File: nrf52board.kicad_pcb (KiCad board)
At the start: 2 copper layers, 10 parts, among them J1 Conn_01x04, U1 nrf52board, U2 E73-2G4M04S

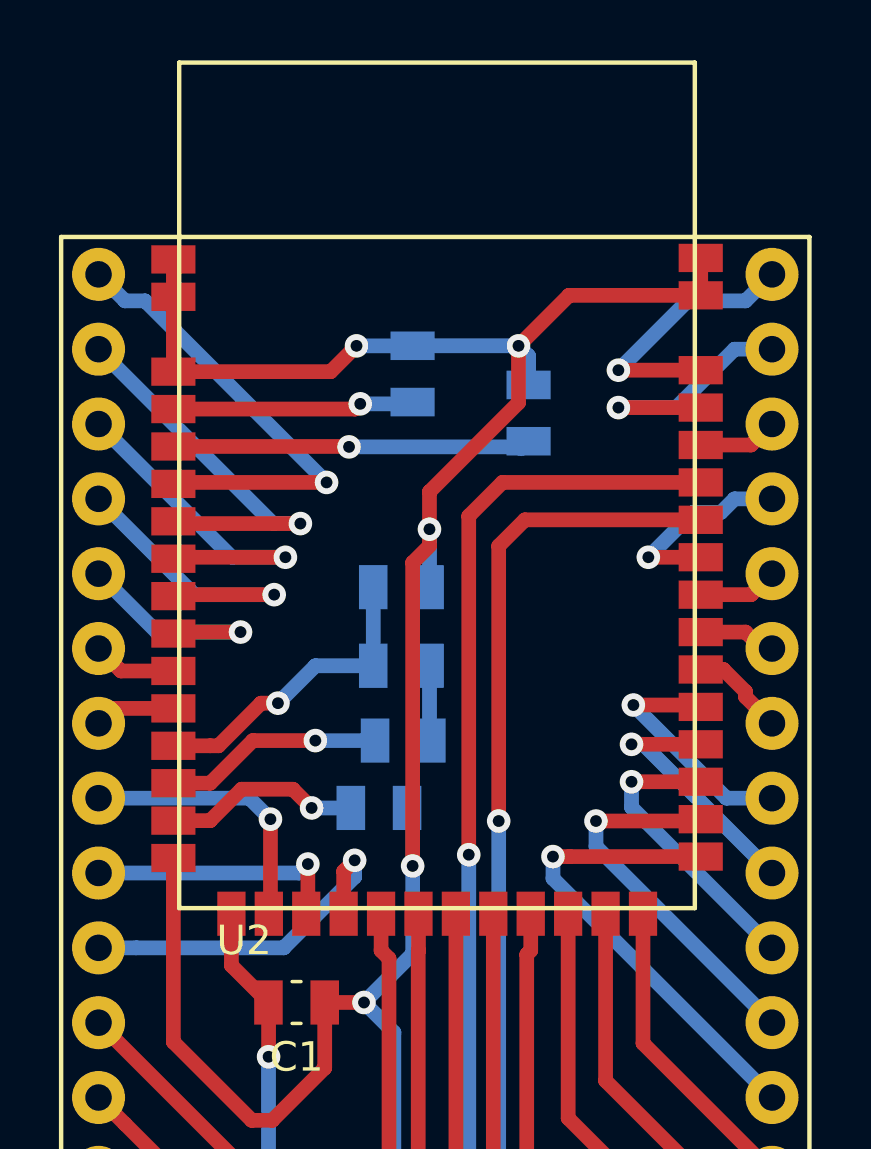
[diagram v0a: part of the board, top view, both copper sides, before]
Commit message: updated module foorptint
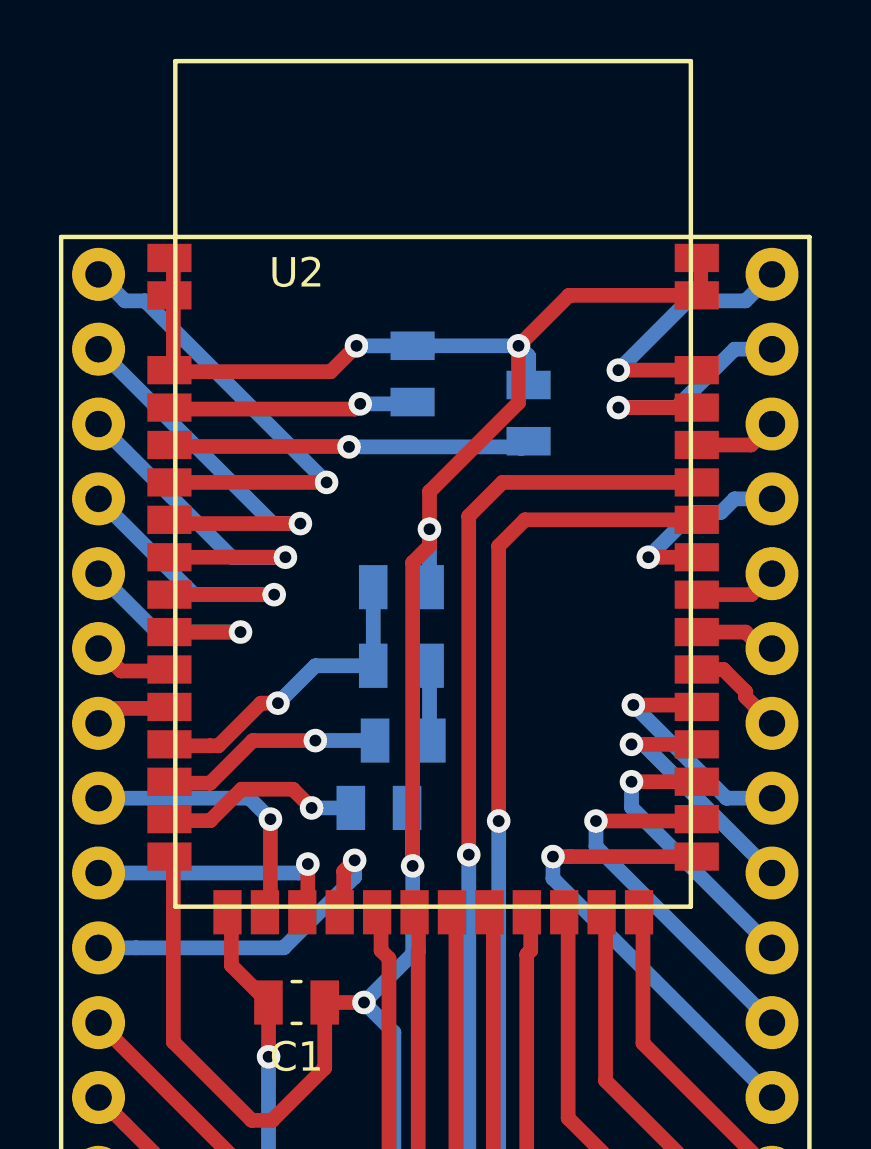
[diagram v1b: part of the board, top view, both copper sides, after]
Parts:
- moved U2 27.2 mm to (62.0, 54.6)

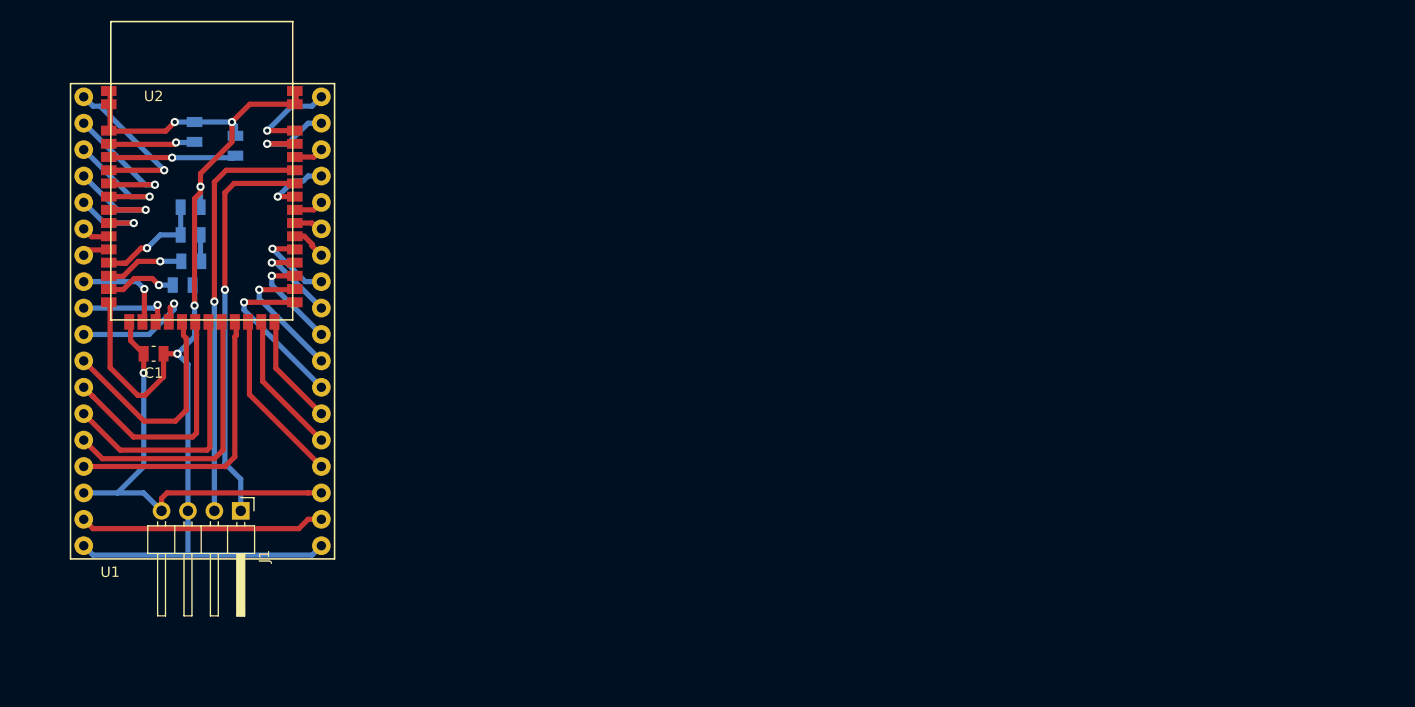
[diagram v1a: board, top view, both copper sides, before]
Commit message: sch: added one more btn and led
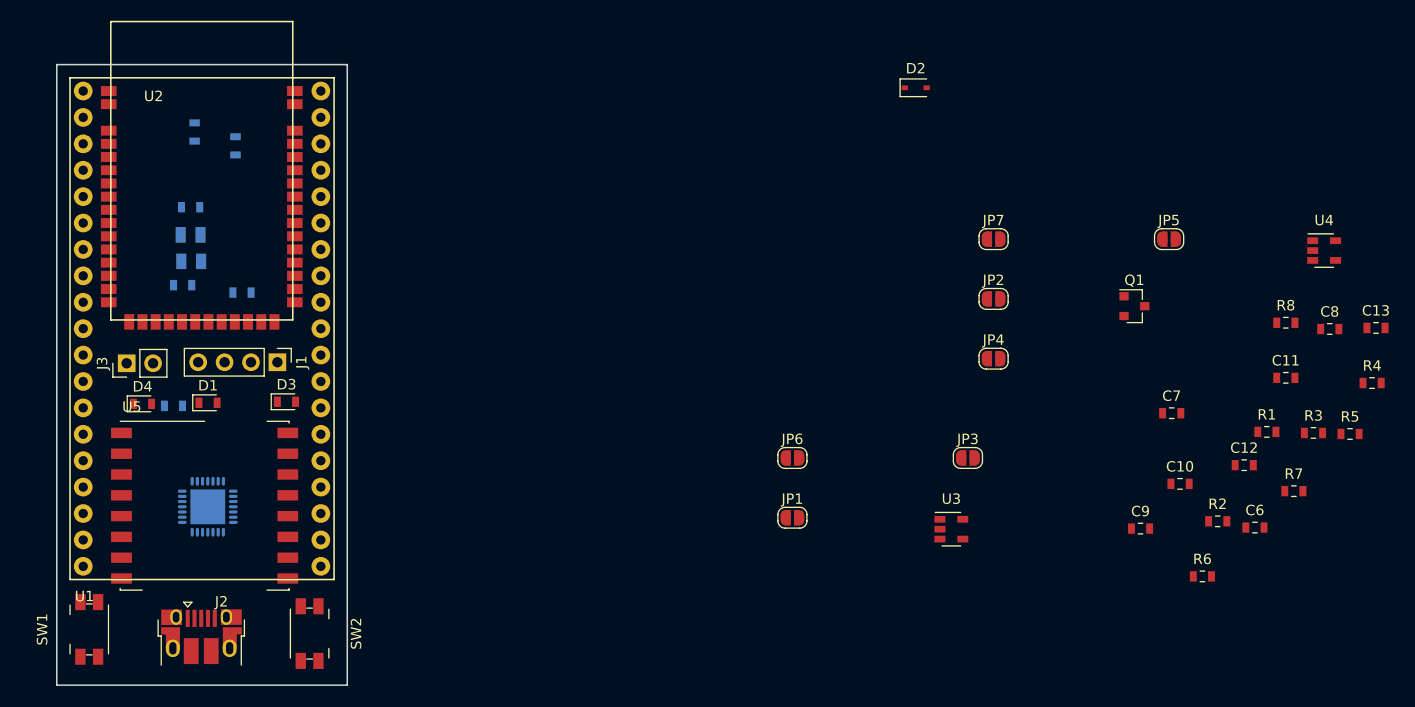
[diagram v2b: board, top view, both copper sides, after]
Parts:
- added C10: 4.7u, Capacitor_SMD:C_0603_1608Metric, F.Cu at (165.0, 92.4)
- added C11: 0.1u, Capacitor_SMD:C_0603_1608Metric, F.Cu at (175.2, 82.2)
- added C12: 0.1u, Capacitor_SMD:C_0603_1608Metric, F.Cu at (171.2, 90.6)
- added C13: 1u, Capacitor_SMD:C_0603_1608Metric, F.Cu at (183.9, 77.4)
- added C6: 4.7u, Capacitor_SMD:C_0603_1608Metric, F.Cu at (172.2, 96.6)
- added C7: 4.7u, Capacitor_SMD:C_0603_1608Metric, F.Cu at (164.2, 85.6)
- added C8: 1u, Capacitor_SMD:C_0603_1608Metric, F.Cu at (179.4, 77.5)
- added C9: 1u, Capacitor_SMD:C_0603_1608Metric, F.Cu at (161.2, 96.7)
- added D1: LED, LED_SMD:LED_0603_1608Metric, F.Cu at (71.5, 84.6)
- added D2: D_Schottky, Diode_SMD:D_SOD-323, F.Cu at (139.6, 54.3)
- added D3: LED, LED_SMD:LED_0603_1608Metric, F.Cu at (79.1, 84.5)
- added D4: LED, LED_SMD:LED_0603_1608Metric, F.Cu at (65.2, 84.7)
- added J2: USB_B_Micro, Connector_USB:USB_Micro-B_Amphenol_10103594-0001LF_Horizontal, F.Cu at (70.9, 107.1)
- added J3: Battery, Connector_PinHeader_2.54mm:PinHeader_1x02_P2.54mm_Vertical, F.Cu at (63.7, 80.8)
- added JP1: SolderJumper_2_Open, Jumper:SolderJumper-2_P1.3mm_Open_RoundedPad1.0x1.5mm, F.Cu at (127.7, 95.7)
- added JP2: SolderJumper_2_Open, Jumper:SolderJumper-2_P1.3mm_Open_RoundedPad1.0x1.5mm, F.Cu at (147.1, 74.6)
- added JP3: SolderJumper_2_Open, Jumper:SolderJumper-2_P1.3mm_Open_RoundedPad1.0x1.5mm, F.Cu at (144.6, 89.9)
- added JP4: SolderJumper_2_Open, Jumper:SolderJumper-2_P1.3mm_Open_RoundedPad1.0x1.5mm, F.Cu at (147.1, 80.4)
- added JP5: SolderJumper_2_Open, Jumper:SolderJumper-2_P1.3mm_Open_RoundedPad1.0x1.5mm, F.Cu at (164.0, 68.9)
- added JP6: SolderJumper_2_Open, Jumper:SolderJumper-2_P1.3mm_Open_RoundedPad1.0x1.5mm, F.Cu at (127.7, 89.9)
- added JP7: SolderJumper_2_Open, Jumper:SolderJumper-2_P1.3mm_Open_RoundedPad1.0x1.5mm, F.Cu at (147.1, 68.9)
- added Q1: Q_PMOS_DSG, Package_TO_SOT_SMD:SOT-23, F.Cu at (160.6, 75.3)
- added R1: 10k, Resistor_SMD:R_0603_1608Metric, F.Cu at (173.4, 87.4)
- added R2: 1M, Resistor_SMD:R_0603_1608Metric, F.Cu at (168.6, 96.0)
- added R3: 470, Resistor_SMD:R_0603_1608Metric, F.Cu at (177.9, 87.5)
- added R4: 100k, Resistor_SMD:R_0603_1608Metric, F.Cu at (183.5, 82.7)
- added R5: 10k, Resistor_SMD:R_0603_1608Metric, F.Cu at (181.4, 87.6)
- added R6: 10k, Resistor_SMD:R_0603_1608Metric, F.Cu at (167.2, 101.3)
- added R7: 10k, Resistor_SMD:R_0603_1608Metric, F.Cu at (176.0, 93.1)
- added R8: 1k, Resistor_SMD:R_0603_1608Metric, F.Cu at (175.2, 76.9)
- added R9: 1k, Resistor_SMD:R_0603_1608Metric, B.Cu at (68.2, 84.9)
- added SW1: SW_Push, Button_Switch_SMD:Panasonic_EVQPUJ_EVQPUA, F.Cu at (60.1, 106.4)
- added SW2: SW_Push, Button_Switch_SMD:Panasonic_EVQPUJ_EVQPUA, F.Cu at (81.3, 106.8)
- added U3: MCP73831-2-OT, Package_TO_SOT_SMD:SOT-23-5, F.Cu at (143.0, 96.8)
- added U4: LP2985-3.3, Package_TO_SOT_SMD:SOT-23-5, F.Cu at (178.9, 70.0)
- added U5: RFM95W-868S2, RF_Module:Hopref_RFM9XW_SMD, F.Cu at (71.2, 94.5)
- added U6: CP2102-GM, Package_DFN_QFN:QFN-28-1EP_5x5mm_P0.5mm_EP3.35x3.35mm, B.Cu at (71.5, 94.6)
- C1: footprint Capacitor_SMD:C_0805_2012Metric -> Capacitor_SMD:C_0603_1608Metric; moved to B.Cu
- C2, C3, C4, C5: footprint Capacitor_SMD:C_0805_2012Metric -> Capacitor_SMD:C_0603_1608Metric
- J1: footprint Connector_PinHeader_2.54mm:PinHeader_1x04_P2.54mm_Horizontal -> Connector_PinHeader_2.54mm:PinHeader_1x04_P2.54mm_Vertical
- moved J1 14.7 mm to (78.2, 80.7)
- moved C1 10.3 mm to (74.8, 74.0)
- moved U1 0.56 mm to (69.8, 77.4)
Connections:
- U1 pad 17: +5V -> GND
- U1 pad 19: GND -> +5V
- U1 pad 21: +3V3 -> GND
- U1 pad 22: P0.10 -> GND
- U1 pad 23: P0.11 -> +3V3
- U1 pad 24: P0.12 -> P0.10
- U1 pad 25: P0.13 -> P0.11
- U1 pad 26: P0.14 -> P0.12
- U1 pad 27: P0.15 -> P0.13
- U1 pad 28: P0.16 -> P0.14
- U1 pad 29: P0.17 -> P0.15
- U1 pad 30: P0.18 -> P0.16
- U1 pad 31: P0.19 -> P0.17
- U1 pad 32: P0.20 -> P0.18
- U1 pad 33: P0.21 -> P0.19
- U1 pad 34: P0.22 -> P0.20
- U1 pad 35: P0.23 -> P0.21
- U1 pad 36: P0.24 -> P0.22
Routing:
- net GND: track 114.2 -> 0.00 mm, vias 5 -> 0
- net +3V3: track 43.0 -> 0.00 mm, vias 1 -> 0
- net Net-(J1-Pad2): track 40.0 -> 0.00 mm, vias 1 -> 0
- net Net-(J1-Pad1): track 38.5 -> 0.00 mm, vias 1 -> 0
- net P0.09: track 27.9 -> 0.00 mm
- net P0.08: track 26.8 -> 0.00 mm
- net P0.07: track 25.7 -> 0.00 mm
- net P0.06: track 23.6 -> 0.00 mm
- net +5V: track 23.6 -> 0.00 mm
- net P0.05: track 21.3 -> 0.00 mm
- net P0.10: track 16.7 -> 0.00 mm
- net P0.13: track 16.3 -> 0.00 mm, vias 1 -> 0
- net P0.25: track 16.0 -> 0.00 mm, vias 1 -> 0
- net P0.11: track 13.7 -> 0.00 mm
- net P0.26: track 13.6 -> 0.00 mm, vias 1 -> 0
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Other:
- board outline added: 27.9 x 59.7 mm

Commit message: pcb: half way through
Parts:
- C11, C12, C13, C6, C7, C8, C9, D2, JP1, JP2, JP3, JP4, JP5, JP6, JP7, Q1, R1, R2, R3, R4, R6, R7, U3, U4: moved to B.Cu
- R9: moved to F.Cu
- moved C13 116.8 mm to (67.6, 88.7), turned to 270 degrees
- moved R5 112.2 mm to (69.2, 84.7)
- moved R4 109.9 mm to (73.9, 90.1), turned to 90 degrees
- moved U4 109.8 mm to (70.7, 88.7), turned to 180 degrees
- moved R3 109.5 mm to (69.7, 104.1), turned to 90 degrees
- moved R1 107.0 mm to (67.6, 104.0), turned to 270 degrees
- moved R7 106.8 mm to (69.2, 93.0), turned to 90 degrees
- moved C6 106.0 mm to (66.4, 101.5)
- moved C11 105.0 mm to (72.4, 104.0)
- moved C8 104.1 mm to (75.8, 87.4), turned to 180 degrees
- moved R8 100.4 mm to (75.1, 85.0), turned to 180 degrees
- moved C12 100.4 mm to (71.2, 99.4)
- moved C7 98.8 mm to (66.4, 99.6)
- moved R6 98.1 mm to (69.2, 96.1), turned to 270 degrees
- moved Q1 96.3 mm to (66.6, 96.1)
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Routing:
- net +5V: track 0.00 -> 61.9 mm, vias 0 -> 3
- net +3V3: track 0.00 -> 48.0 mm, vias 0 -> 4
- net P0.08: track 0.00 -> 29.5 mm, vias 0 -> 4
- net P0.21: track 0.00 -> 26.5 mm, vias 0 -> 1
- net P0.18: track 0.00 -> 25.2 mm, vias 0 -> 2
- net P0.09: track 0.00 -> 25.0 mm, vias 0 -> 1
- net Net-(JP4-Pad1): track 0.00 -> 24.3 mm, vias 0 -> 1
- net P0.17: track 0.00 -> 23.6 mm, vias 0 -> 1
- net P0.27: track 0.00 -> 23.5 mm, vias 0 -> 1
- net P0.26: track 0.00 -> 23.2 mm, vias 0 -> 1
- net Net-(JP5-Pad1): track 0.00 -> 19.9 mm, vias 0 -> 1
- net Net-(C8-Pad2): track 0.00 -> 17.9 mm
- net P0.07: track 0.00 -> 17.6 mm
- net P0.10: track 0.00 -> 16.3 mm
- net Net-(JP6-Pad1): track 0.00 -> 15.8 mm, vias 0 -> 1
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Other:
- net class Default: trace_width 0.5 -> 0.2; via_dia 0.8 -> 0.6; via_drill 0.4 -> 0.3
- net class power added: clearance 0.2, trace_width 0.4, via_dia 0.6, via_drill 0.3

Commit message: pcb: almost done
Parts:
- moved JP7 1.19 mm to (76.9, 100.6), turned to 270 degrees
- moved C12 0.92 mm to (70.3, 99.4)
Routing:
- net P0.24: track 4.85 -> 129.9 mm, vias 0 -> 1
- net P0.25: track 11.0 -> 74.4 mm, vias 1 -> 3
- net P0.23: track 4.13 -> 62.0 mm, vias 0 -> 1
- net P0.21: track 26.5 -> 73.4 mm
- net P0.06: track 14.5 -> 54.3 mm, vias 0 -> 2
- net P0.22: track 3.03 -> 42.2 mm
- net P0.13: track 8.66 -> 37.8 mm, vias 2 -> 3
- net P0.07: track 17.6 -> 46.4 mm, vias 0 -> 2
- net P0.05: track 11.4 -> 40.0 mm, vias 0 -> 4
- net P0.27: track 23.5 -> 48.6 mm, vias 1 -> 2
- net P0.08: track 29.5 -> 52.3 mm, vias 4 -> 2
- net P0.26: track 23.2 -> 45.7 mm, vias 1 -> 2
- net +3V3: track 48.0 -> 70.4 mm, vias 4 -> 5
- net Net-(J1-Pad2): track 0.00 -> 22.0 mm, vias 0 -> 1
- net Net-(J1-Pad1): track 0.00 -> 19.6 mm, vias 0 -> 1
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
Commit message: pcb: traciong done
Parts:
- R2: moved to F.Cu
- moved R2 4.29 mm to (78.6, 104.1)
- moved U3 0.58 mm to (64.3, 105.0)
- moved R1 0.41 mm to (67.3, 104.1), turned to 90 degrees
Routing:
- net P0.24: track 129.9 -> 55.1 mm
- net GND: track 4.82 -> 77.9 mm, vias 0 -> 91
- net Net-(J2-Pad6): track 0.00 -> 18.7 mm
- net P0.23: track 62.0 -> 49.0 mm, vias 1 -> 0
- net P0.06: track 54.3 -> 51.6 mm
- net Net-(R1-Pad2): track 0.00 -> 2.61 mm
- net Net-(L1-Pad2): track 0.00 -> 2.35 mm
- net Net-(R3-Pad2): track 5.72 -> 8.07 mm, vias 0 -> 2
- net Net-(C8-Pad2): track 17.8 -> 19.7 mm, vias 0 -> 4
- net P0.22: track 42.2 -> 40.3 mm
- net +3V3: track 70.4 -> 69.2 mm, vias 5 -> 6
- net P0.25: track 74.4 -> 73.3 mm
- net Net-(JP3-Pad1): track 7.80 -> 8.79 mm
- net P0.08: track 52.3 -> 51.4 mm, vias 2 -> 4
- net P0.13: track 37.8 -> 37.1 mm
- added copper zone on B.Cu, net GND
- added copper zone on F.Cu, net GND

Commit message: pcb: done
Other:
- board text added: "github.com/ dimka-rs/ nrf52board rev.1"
